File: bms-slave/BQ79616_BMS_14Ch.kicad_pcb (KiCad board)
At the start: 4 copper layers, 140 x 70 mm, 173 parts, among them J1 Conn_Therm, J2 Conn_02x10_Odd_Even, J3 Conn_02x10_Odd_Even, J4 BMS_A_OUT, J5 BMS_A_IN, Q1 MMBT5551, Q10 DMN2024UQ, Q11 DMN2024UQ, Q12 DMN2024UQ, Q13 DMN2024UQ, Q14 DMN2024UQ, Q15 DMN2024UQ, Q2 DMN2024UQ, Q3 DMN2024UQ, Q4 DMN2024UQ, Q5 DMN2024UQ, Q6 DMN2024UQ, Q7 DMN2024UQ, Q8 DMN2024UQ, Q9 DMN2024UQ

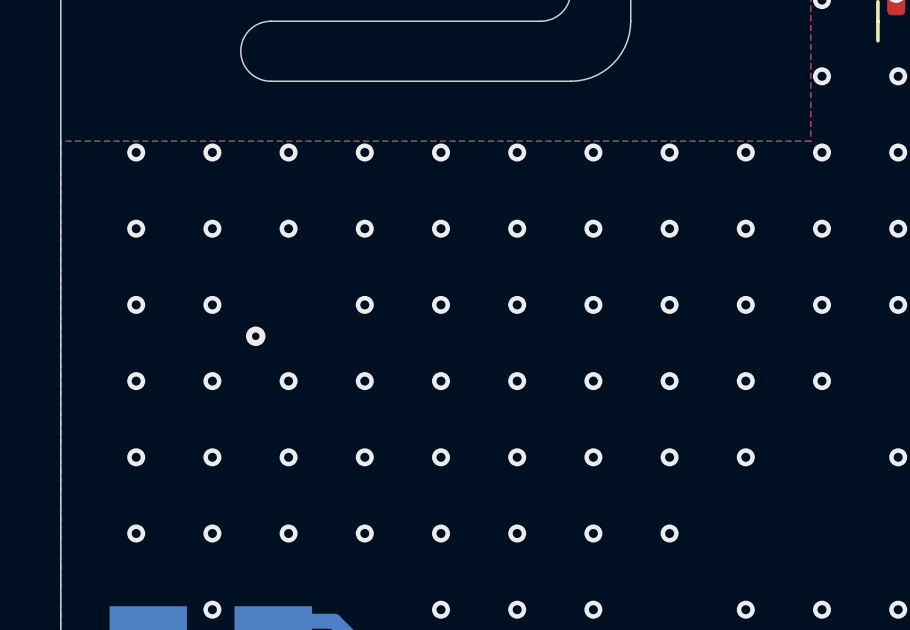
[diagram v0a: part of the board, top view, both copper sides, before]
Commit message: Add team logo to the board
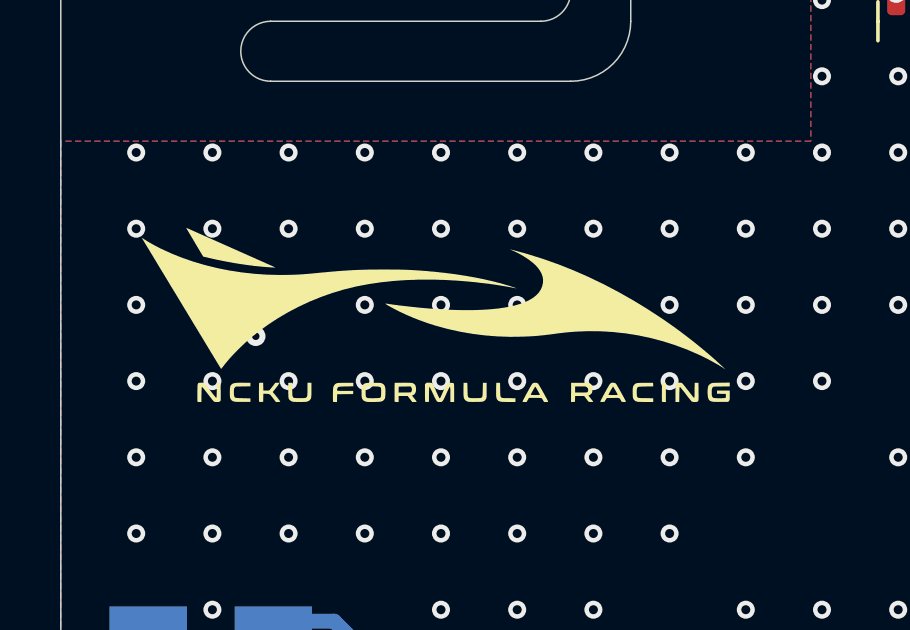
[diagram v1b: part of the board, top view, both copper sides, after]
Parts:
- added G***: LOGO, LOGO, F.Cu at (92.5, 90.8)

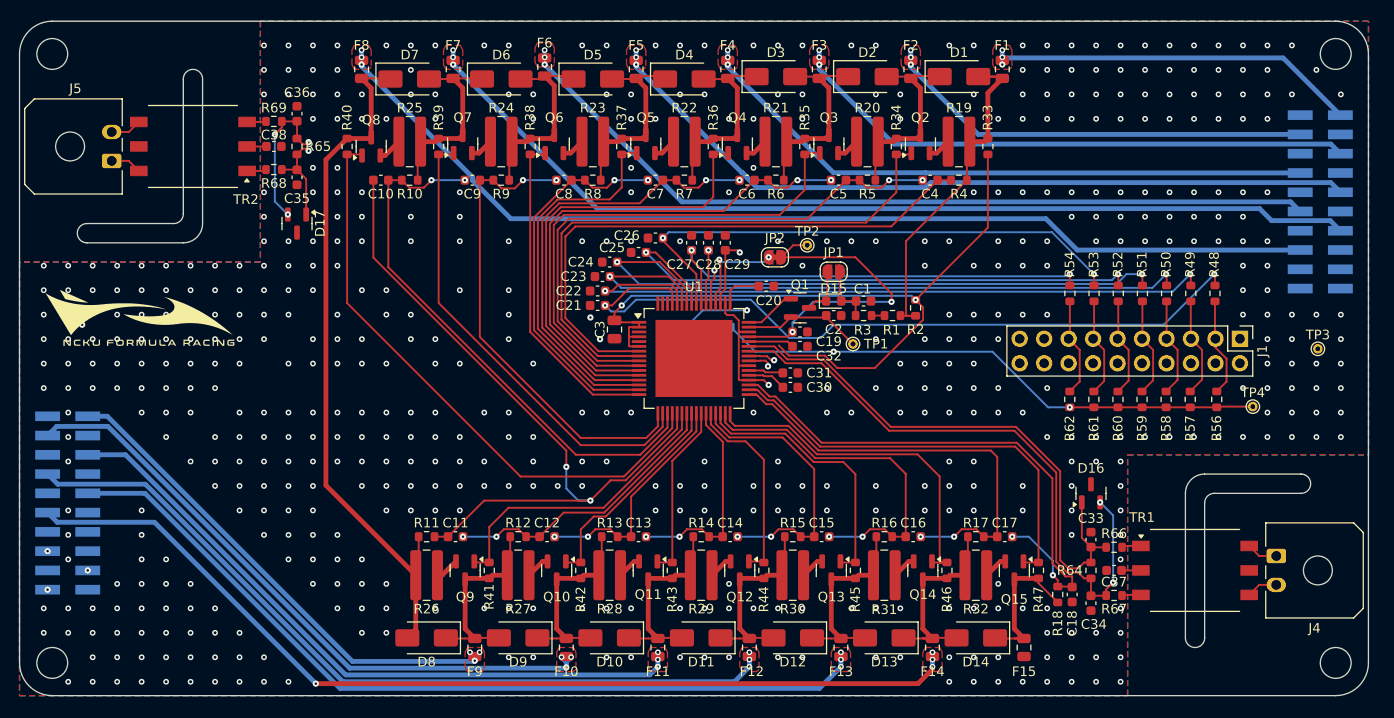
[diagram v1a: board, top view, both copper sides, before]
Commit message: Add label of connectors, test points
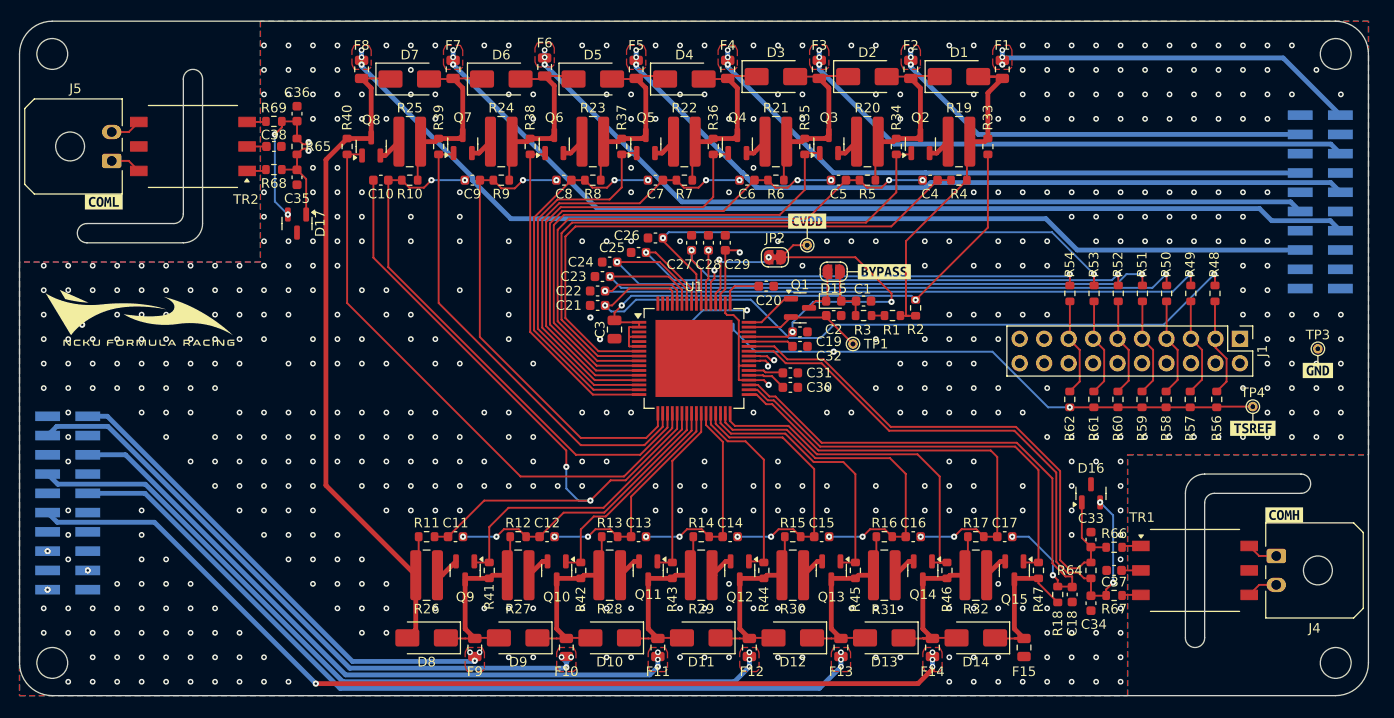
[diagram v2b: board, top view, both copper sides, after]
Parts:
- added kibuzzard-67C80B11: G***, kibuzzard-67C80B11, F.Cu at (211.2, 111.2)
- added kibuzzard-67C80B29: G***, kibuzzard-67C80B29, F.Cu at (88.8, 78.8)
- added kibuzzard-67C80B8B: G***, kibuzzard-67C80B8B, F.Cu at (161.8, 80.8)
- added kibuzzard-67C80BF3: G***, kibuzzard-67C80BF3, F.Cu at (214.8, 96.2)
- added kibuzzard-67C80C10: G***, kibuzzard-67C80C10, F.Cu at (208.0, 102.2)
- added kibuzzard-67C80F0F: G***, kibuzzard-67C80F0F, F.Cu at (169.8, 86.0)
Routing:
- net /BAT_A: track 79.8 -> 59.4 mm

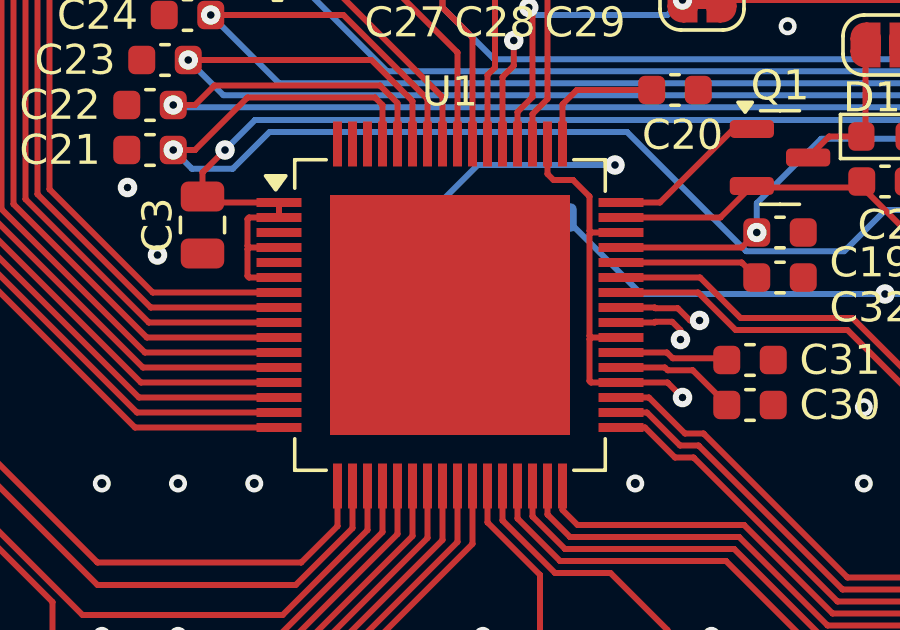
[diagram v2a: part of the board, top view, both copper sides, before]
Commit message: Connect main chip's pad to GND and put vias through holes
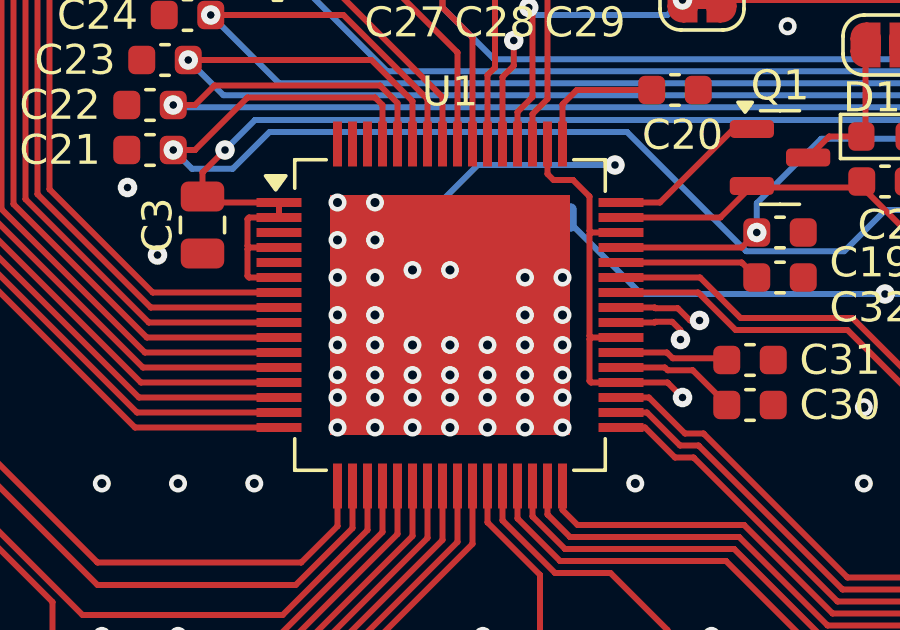
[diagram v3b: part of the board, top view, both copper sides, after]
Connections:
- U1 pad 65: (no net) -> GND1
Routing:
- net GND1: vias 562 -> 604

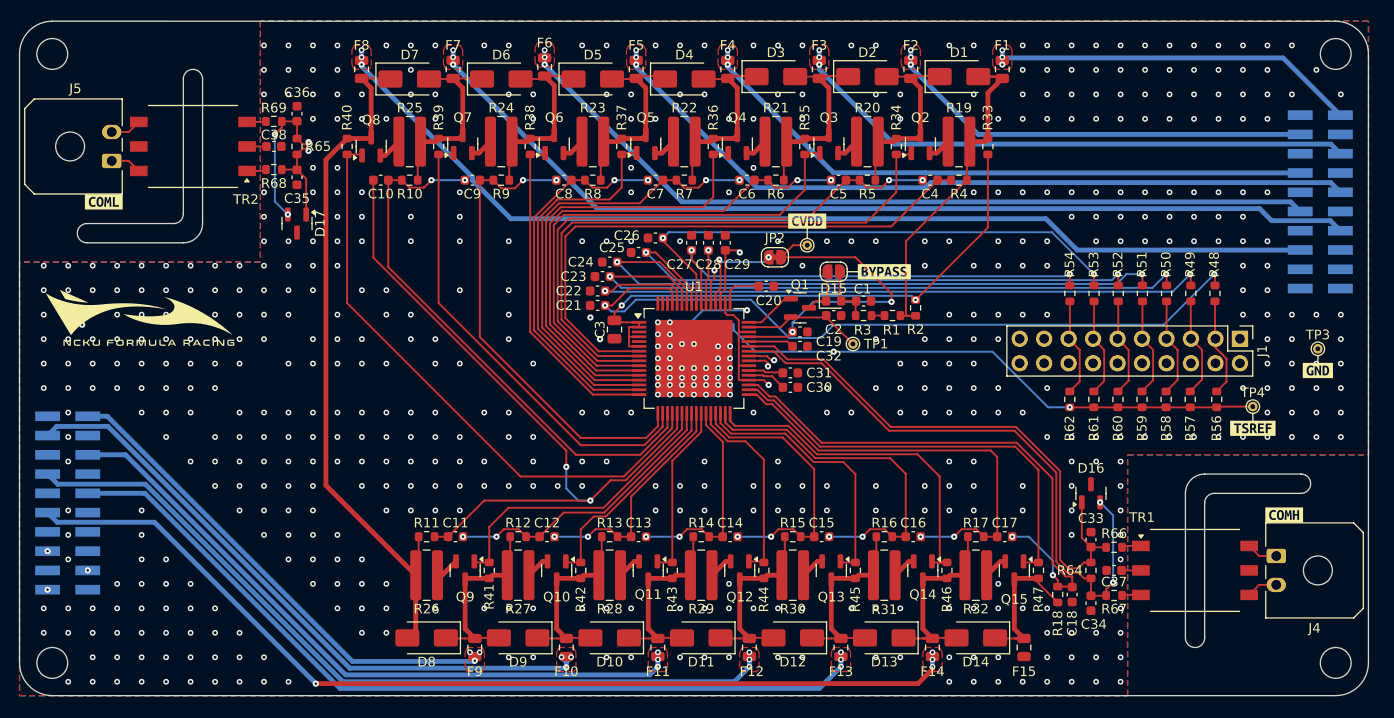
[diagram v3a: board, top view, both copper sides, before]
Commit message: feat: improve bms thermal performance
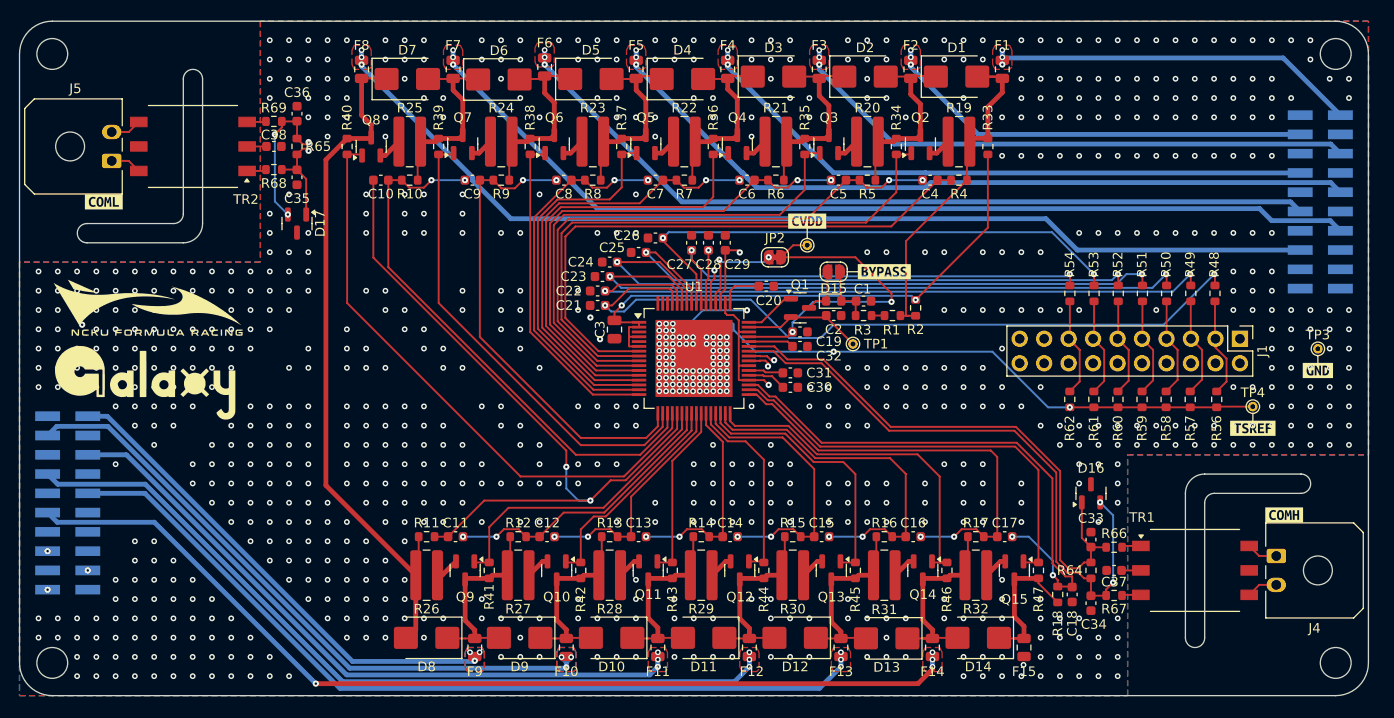
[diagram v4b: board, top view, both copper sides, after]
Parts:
- removed the G*** at (92.5, 90.8)
- added G***: LOGO, logo:nckufs_logo_20mm, F.Cu at (93.3, 89.7)
- added G***: LOGO, logo:galaxy_logo_20mm, F.Cu at (93.2, 97.5)
- D1, D10, D11, D12, D13, D14, D2, D3, D4, D5, D6, D7, D8, D9: value SMA6J5.0CAQ -> SMBJ55.0CA; footprint Diode_SMD:D_SMA -> Diode_SMD:D_SMB
- moved D13 0.25 mm to (170.0, 124.0)
- moved D6 0.25 mm to (129.8, 66.0)
- moved D1 0.25 mm to (177.2, 65.8)
- moved D11 0.25 mm to (151.0, 124.0)
- moved D12 0.25 mm to (160.5, 124.0)
- moved D14 0.25 mm to (179.5, 124.0)
- moved D2 0.25 mm to (167.8, 65.8)
- moved D3 0.25 mm to (158.2, 65.8)
- moved D7 0.25 mm to (120.2, 66.0)
- moved D10 0.20 mm to (141.4, 124.0)
- moved D4 0.20 mm to (148.8, 66.0)
- moved D5 0.20 mm to (139.3, 66.0)
- moved D9 0.15 mm to (131.9, 124.0)
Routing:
- net GND1: vias 604 -> 913
- added copper zone on B.Cu, net /CELL_A5
- added copper zone on B.Cu, net /CELL_A6

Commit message: fix: improve GND plant
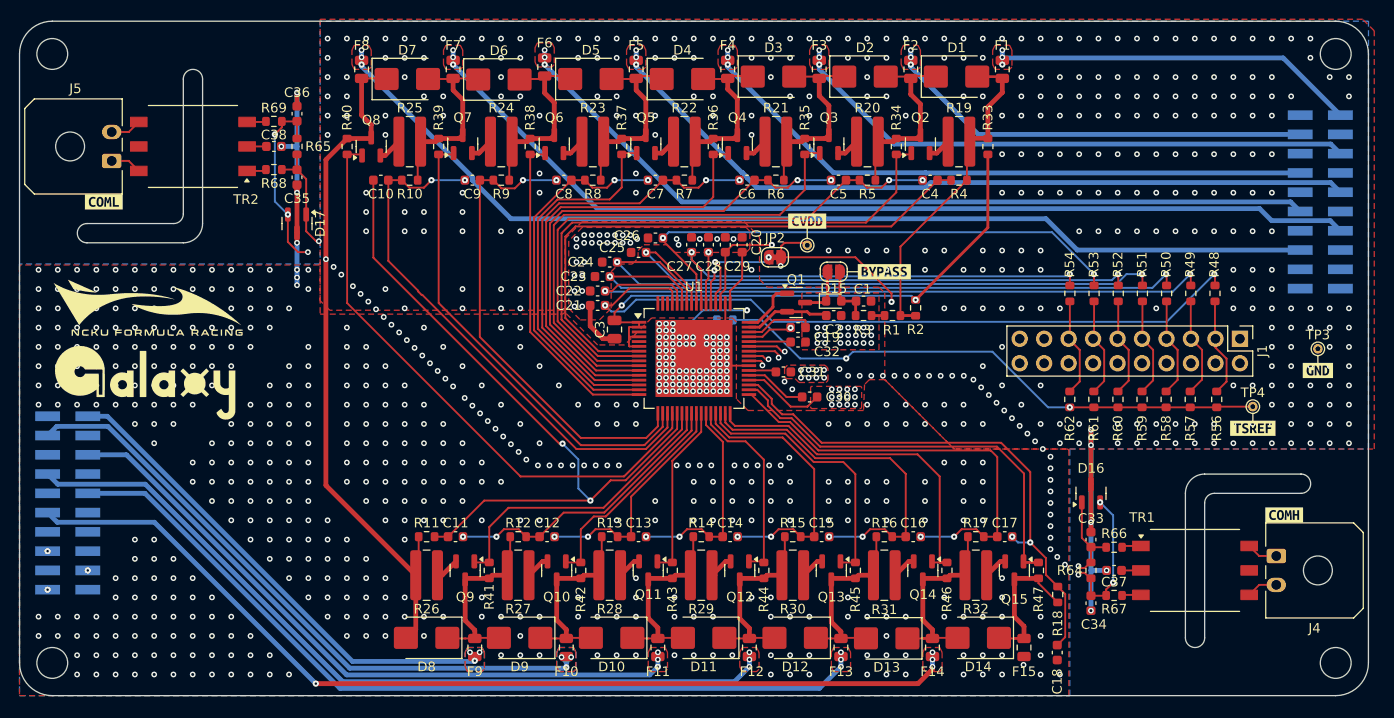
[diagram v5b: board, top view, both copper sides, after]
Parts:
- removed TP1: TestPoint, TestPoint:TestPoint_THTPad_D1.0mm_Drill0.5mm
- moved C18 6.22 mm to (187.7, 125.5)
- moved C20 4.97 mm to (155.0, 83.2), turned to 90 degrees
- moved C30 2.24 mm to (162.0, 99.0)
- moved R63 0.78 mm to (153.2, 91.0)
- moved C31 0.73 mm to (159.3, 96.4)
- moved Q1 0.68 mm to (160.6, 89.2)
- moved C19 0.49 mm to (160.8, 91.8)
- moved C32 0.49 mm to (160.8, 93.3)
- moved C27 0.20 mm to (149.8, 83.2)
- moved C28 0.20 mm to (151.5, 83.2)
- moved C29 0.20 mm to (153.2, 83.2)
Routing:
- net GND1: track 14.3 -> 87.3 mm, vias 913 -> 1028
- net /COMLN: track 81.4 -> 94.2 mm
- net /COMLP: track 75.2 -> 82.3 mm
- net /TSREF_A: track 79.3 -> 84.4 mm
- net /LDOIN_A: track 12.7 -> 9.03 mm
- net /VC_A0: track 57.7 -> 55.3 mm
- net /REFHP_A: track 4.06 -> 6.46 mm
- net Net-(D1-A2): track 35.9 -> 38.3 mm
- net /CVDD_A: track 124.7 -> 122.9 mm, vias 3 -> 4
- net /DVDD_A: track 4.50 -> 5.97 mm
- net /GPIO_A1: track 78.7 -> 77.3 mm
- net /COMHN: track 64.6 -> 65.4 mm, vias 2 -> 4
- net /VC_A8: track 57.3 -> 56.5 mm
- net /AVDD_A: track 3.63 -> 2.86 mm
- net /VC_A7: track 74.7 -> 74.2 mm
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- added copper zone on In1.Cu, net GND1
- added copper zone on In2.Cu, net GND1
